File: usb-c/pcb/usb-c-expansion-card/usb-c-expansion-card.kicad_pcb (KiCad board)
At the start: 2 copper layers, 26 x 30 mm, 11 parts, among them P1 USB_C_Plug_USB2.0, U1 AP2112K-3.3

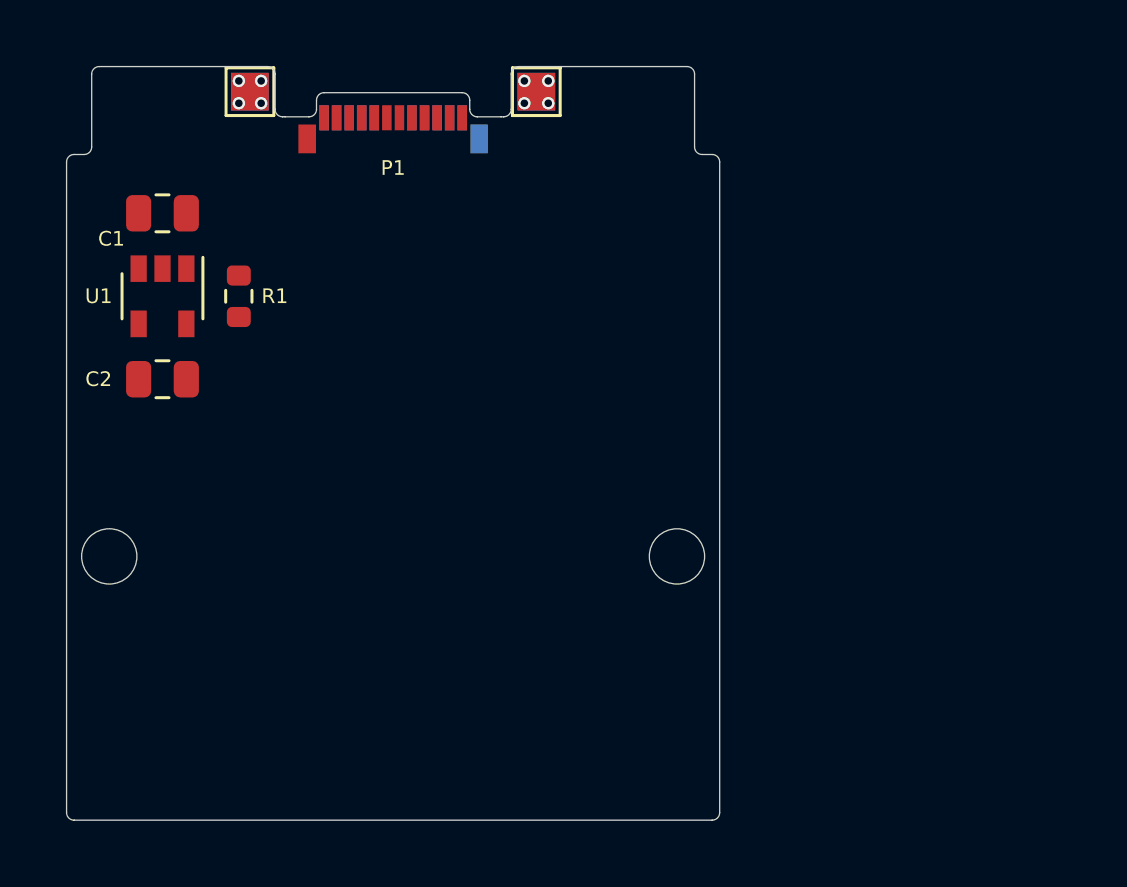
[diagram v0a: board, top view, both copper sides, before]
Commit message: Begin routing PCB
Signed-off-by: Lucy <user@domain.tld>
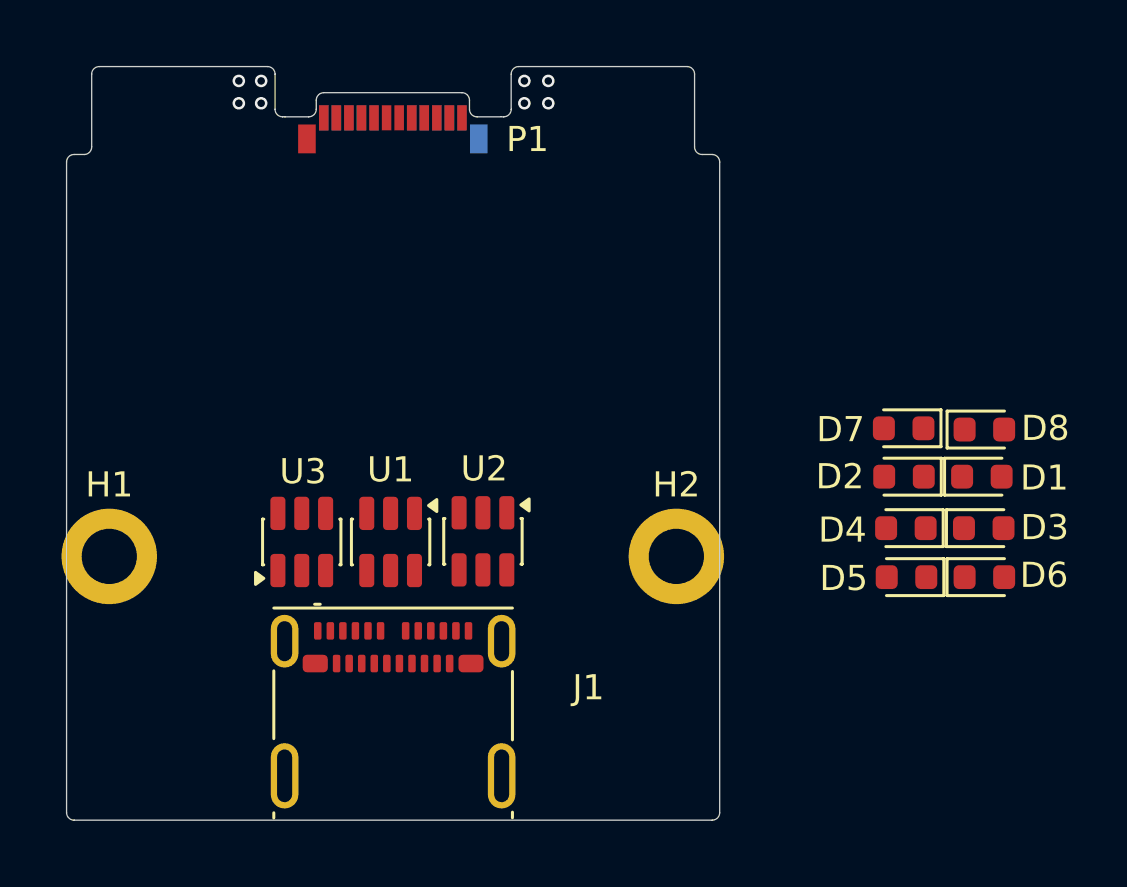
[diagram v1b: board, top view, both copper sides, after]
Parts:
- removed C1, C2: 10uF, Capacitor_SMD:C_0805_2012Metric
- removed R1: 5.1k, Resistor_SMD:R_0603_1608Metric
- removed TP1, TP2, TP3, TP4: TestPoint, TestPoint:TestPoint_Pad_1.5x1.5mm
- added D1: AZ5B0S-01F, Diode_SMD:D_0603_1608Metric, F.Cu at (163.4, 143.3)
- added D2: AZ5B0S-01F, Diode_SMD:D_0603_1608Metric, F.Cu at (160.3, 143.3)
- added D3: AZ5B0S-01F, Diode_SMD:D_0603_1608Metric, F.Cu at (163.5, 145.4)
- added D4: AZ5B0S-01F, Diode_SMD:D_0603_1608Metric, F.Cu at (160.4, 145.4)
- added D5: AZ5B0S-01F, Diode_SMD:D_0603_1608Metric, F.Cu at (160.4, 147.3)
- added D6: AZ5B0S-01F, Diode_SMD:D_0603_1608Metric, F.Cu at (163.5, 147.3)
- added D7: AZ5B0S-01F, Diode_SMD:D_0603_1608Metric, F.Cu at (160.3, 141.4)
- added D8: AZ5B0S-01F, Diode_SMD:D_0603_1608Metric, F.Cu at (163.5, 141.4)
- added J1: USB_C_Receptacle, Connector_USB:USB_C_Receptacle_Molex_105450-0101, F.Cu at (140.0, 152.7)
- added U2: USBLC6-2SC6, Package_TO_SOT_SMD:SOT-23-6, F.Cu at (143.6, 145.9)
- added U3: USBLC6-2SC6, Package_TO_SOT_SMD:SOT-23-6, F.Cu at (136.4, 145.9)
- H1, H2: footprint MountingHole:MountingHole_2.2mm_M2 -> MountingHole:MountingHole_2.2mm_M2_DIN965_Pad
- P1: value USB_C_Plug_USB2.0 -> USB_C_Plug
- U1: value AP2112K-3.3 -> USBLC6-2SC6; footprint Package_TO_SOT_SMD:SOT-23-5 -> Package_TO_SOT_SMD:SOT-23-6
- moved U1 13.3 mm to (139.9, 145.9)
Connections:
- P1 pad A10: (no net) -> /RX2N_ESD
- P1 pad A11: (no net) -> /RX2P_ESD
- P1 pad A2: (no net) -> /TX1P_ESD
- P1 pad A3: (no net) -> /TX1N_ESD
- P1 pad A4: VBUS -> /VBUS
- P1 pad A6: (no net) -> Net-(P1-D+)
- P1 pad A7: (no net) -> Net-(P1-D-)
- P1 pad A8: (no net) -> Net-(P1-SBU1)
- P1 pad A9: VBUS -> /VBUS
- P1 pad B10: (no net) -> /RX1N_ESD
- P1 pad B11: (no net) -> /RX1P_ESD
- P1 pad B2: (no net) -> /TX2P_ESD
- P1 pad B3: (no net) -> /TX2N_ESD
- P1 pad B4: VBUS -> /VBUS
- P1 pad B5: (no net) -> Net-(P1-VCONN)
- P1 pad B8: (no net) -> Net-(P1-SBU2)
- P1 pad B9: VBUS -> /VBUS
- P1 pad S1: GND -> (no net)
- U1 pad 1: VBUS -> Net-(P1-D-)
- U1 pad 3: VBUS -> Net-(P1-D+)
- U1 pad 4: (no net) -> Net-(J1-D+-PadA6)
- U1 pad 5: +3V3 -> unconnected-(U1-VBUS-Pad5)
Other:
- copper layers 2 -> 4
- net class Default removed

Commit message: Update net labels for differential pair routing
Signed-off-by: Lucy <user@domain.tld>
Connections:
- net /RX1N_ESD renamed /ESD_RX1_N
- net /RX1P_ESD renamed /ESD_RX1_P
- net /RX2N_ESD renamed /ESD_RX2_N
- net /RX2P_ESD renamed /ESD_RX2_P
- net /TX1N_ESD renamed /ESD_TX1_N
- net /TX1P_ESD renamed /ESD_TX1_P
- net /TX2N_ESD renamed /ESD_TX2_N
- net /TX2P_ESD renamed /ESD_TX2_P
- net Net-(J1-CC1) renamed /CC1
- net Net-(J1-CC2) renamed /CC2
- net Net-(J1-D+-PadA6) renamed /IN_D_P
- net Net-(J1-D--PadA7) renamed /IN_D_N
- net Net-(J1-SBU1) renamed /IN_SBU1
- net Net-(J1-SBU2) renamed /IN_SBU2
- net Net-(P1-CC) renamed /CC
- net Net-(P1-D+) renamed /OUT_D_P
- net Net-(P1-D-) renamed /OUT_D_N
- net Net-(P1-SBU1) renamed /OUT_SBU1
- net Net-(P1-SBU2) renamed /OUT_SBU2
- net Net-(P1-VCONN) renamed /VCONN
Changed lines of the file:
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@@
 		(13 "F.Paste" user)
 		(15 "B.Paste" user)
-		(5 "F.SilkS" user)
-		(7 "B.SilkS" user)
+		(5 "F.SilkS" user "F.Silkscreen")
+		(7 "B.SilkS" user "B.Silkscreen")
 		(1 "F.Mask" user)
 		(3 "B.Mask" user)
 		(25 "Edge.Cuts" user)
 		(27 "Margin" user)
-		(31 "F.CrtYd" user)
-		(29 "B.CrtYd" user)
+		(31 "F.CrtYd" user "F.Courtyard")
+		(29 "B.CrtYd" user "B.Courtyard")
 		(35 "F.Fab" user)
 	)
@@
 		(capping no)
 		(filling no)
-		(zone_defaults)
 		(pcbplotparams
 			(layerselection 0x00000000_00000000_55555555_57555550)
@@
 			(layers "F.Cu" "F.Mask" "F.Paste")
 			(roundrect_rratio 0.25)
-			(net "/TX1P_ESD")
+			(net "/ESD_TX1_P")
 			(pinfunction "A1_1")
 			(pintype "passive")
@@
 			(layers "F.Cu" "F.Mask" "F.Paste")
 			(roundrect_rratio 0.25)
-			(net "/RX1N_ESD")
+			(net "/ESD_RX1_N")
 			(pinfunction "A1_1")
 			(pintype "passive")
@@
 			(layers "F.Cu" "F.Mask" "F.Paste")
 			(roundrect_rratio 0.25)
-			(net "/TX2N_ESD")
+			(net "/ESD_TX2_N")
 			(pinfunction "A1_1")
 			(pintype "passive")
@@
 			(layers "F.Cu" "F.Mask" "F.Paste")
 			(roundrect_rratio 0.25)
-			(net "/TX1P_ESD")
+			(net "/ESD_TX1_P")
 			(pinfunction "TX1+_A2")
 			(pintype "bidirectional")
@@
 			(layers "F.Cu" "F.Mask" "F.Paste")
 			(roundrect_rratio 0.25)
-			(net "/TX1N_ESD")
+			(net "/ESD_TX1_N")
 			(pinfunction "TX1-_A3")
 			(pintype "bidirectional")
@@
 			(layers "F.Cu" "F.Mask" "F.Paste")
 			(roundrect_rratio 0.25)
-			(net "Net-(J1-CC1)")
+			(net "/CC1")
 			(pinfunction "CC1_A5")
 			(pintype "bidirectional")
@@
 			(layers "F.Cu" "F.Mask" "F.Paste")
 			(roundrect_rratio 0.25)
-			(net "Net-(J1-D+-PadA6)")
+			(net "/IN_D_P")
 			(pinfunction "D+_A6")
 			(pintype "bidirectional")
@@
 			(layers "F.Cu" "F.Mask" "F.Paste")
 			(roundrect_rratio 0.25)
-			(net "Net-(J1-D--PadA7)")
+			(net "/IN_D_N")
 			(pinfunction "D-_A7")
 			(pintype "bidirectional")
@@
 			(layers "F.Cu" "F.Mask" "F.Paste")
 			(roundrect_rratio 0.25)
-			(net "Net-(J1-SBU1)")
+			(net "/IN_SBU1")
 			(pinfunction "SBU1_A8")
 			(pintype "bidirectional")
@@
 			(layers "F.Cu" "F.Mask" "F.Paste")
 			(roundrect_rratio 0.25)
-			(net "/RX2N_ESD")
+			(net "/ESD_RX2_N")
 			(pinfunction "RX2-_A10")
 			(pintype "bidirectional")
@@
 			(layers "F.Cu" "F.Mask" "F.Paste")
 			(roundrect_rratio 0.25)
-			(net "/RX2P_ESD")
+			(net "/ESD_RX2_P")
 			(pinfunction "RX2+_A11")
 			(pintype "bidirectional")
@@
 			(layers "F.Cu" "F.Mask" "F.Paste")
 			(roundrect_rratio 0.25)
-			(net "/TX2P_ESD")
+			(net "/ESD_TX2_P")
 			(pinfunction "TX2+_B2")
 			(pintype "bidirectional")
@@
 			(layers "F.Cu" "F.Mask" "F.Paste")
 			(roundrect_rratio 0.25)
-			(net "/TX2N_ESD")
+			(net "/ESD_TX2_N")
 			(pinfunction "TX2-_B3")
 			(pintype "bidirectional")
@@
 			(layers "F.Cu" "F.Mask" "F.Paste")
 			(roundrect_rratio 0.25)
-			(net "Net-(J1-CC2)")
+			(net "/CC2")
 			(pinfunction "CC2_B5")
 			(pintype "bidirectional")
@@
 			(layers "F.Cu" "F.Mask" "F.Paste")
 			(roundrect_rratio 0.25)
-			(net "Net-(J1-D+-PadA6)")
+			(net "/IN_D_P")
 			(pinfunction "D+_B6")
 			(pintype "bidirectional")
@@
 			(layers "F.Cu" "F.Mask" "F.Paste")
 			(roundrect_rratio 0.25)
-			(net "Net-(J1-D--PadA7)")
+			(net "/IN_D_N")
 			(pinfunction "D-_B7")
 			(pintype "bidirectional")
@@
 			(layers "F.Cu" "F.Mask" "F.Paste")
 			(roundrect_rratio 0.25)
-			(net "Net-(J1-SBU2)")
+			(net "/IN_SBU2")
 			(pinfunction "SBU2_B8")
 			(pintype "bidirectional")
@@
 			(layers "F.Cu" "F.Mask" "F.Paste")
 			(roundrect_rratio 0.25)
-			(net "/RX1N_ESD")
+			(net "/ESD_RX1_N")
 			(pinfunction "RX1-_B10")
 			(pintype "bidirectional")
@@
 			(layers "F.Cu" "F.Mask" "F.Paste")
 			(roundrect_rratio 0.25)
-			(net "/RX1P_ESD")
+			(net "/ESD_RX1_P")
 			(pinfunction "RX1+_B11")
 			(pintype "bidirectional")
@@
 			(size 0.38 1)
 			(layers "F.Cu" "F.Mask" "F.Paste")
-			(net "/TX1P_ESD")
+			(net "/ESD_TX1_P")
 			(pinfunction "TX1+_A2")
 			(pintype "bidirectional")
@@
 			(size 0.38 1)
 			(layers "F.Cu" "F.Mask" "F.Paste")
-			(net "/TX1N_ESD")
+			(net "/ESD_TX1_N")
 			(pinfunction "TX1-_A3")
 			(pintype "bidirectional")
@@
 			(size 0.38 1)
 			(layers "F.Cu" "F.Mask" "F.Paste")
-			(net "Net-(P1-CC)")
+			(net "/CC")
 			(pinfunction "CC_A5")
 			(pintype "bidirectional")
@@
 			(size 0.38 1)
 			(layers "F.Cu" "F.Mask" "F.Paste")
-			(net "Net-(P1-D+)")
+			(net "/OUT_D_P")
 			(pinfunction "D+_A6")
 			(pintype "bidirectional")
@@
 			(size 0.38 1)
 			(layers "F.Cu" "F.Mask" "F.Paste")
-			(net "Net-(P1-D-)")
+			(net "/OUT_D_N")
 			(pinfunction "D-_A7")
 			(pintype "bidirectional")
@@
 			(size 0.38 1)
 			(layers "F.Cu" "F.Mask" "F.Paste")
-			(net "Net-(P1-SBU1)")
+			(net "/OUT_SBU1")
 			(pinfunction "SBU1_A8")
 			(pintype "bidirectional")
@@
 			(size 0.38 1)
 			(layers "F.Cu" "F.Mask" "F.Paste")
-			(net "/RX2N_ESD")
+			(net "/ESD_RX2_N")
 			(pinfunction "RX2-_A10")
 			(pintype "bidirectional")
@@
 			(size 0.38 1)
 			(layers "F.Cu" "F.Mask" "F.Paste")
-			(net "/RX2P_ESD")
+			(net "/ESD_RX2_P")
 			(pinfunction "RX2+_A11")
 			(pintype "bidirectional")
@@
 			(size 0.38 1)
 			(layers "B.Cu" "B.Mask" "B.Paste")
-			(net "/TX2P_ESD")
+			(net "/ESD_TX2_P")
 			(pinfunction "TX2+_B2")
 			(pintype "bidirectional")
@@
 			(size 0.38 1)
 			(layers "B.Cu" "B.Mask" "B.Paste")
-			(net "/TX2N_ESD")
+			(net "/ESD_TX2_N")
 			(pinfunction "TX2-_B3")
 			(pintype "bidirectional")
@@
 			(size 0.38 1)
 			(layers "B.Cu" "B.Mask" "B.Paste")
-			(net "Net-(P1-VCONN)")
+			(net "/VCONN")
 			(pinfunction "VCONN_B5")
 			(pintype "bidirectional")
@@
 			(size 0.38 1)
 			(layers "B.Cu" "B.Mask" "B.Paste")
-			(net "Net-(P1-SBU2)")
+			(net "/OUT_SBU2")
 			(pinfunction "SBU2_B8")
 			(pintype "bidirectional")
@@
 			(size 0.38 1)
 			(layers "B.Cu" "B.Mask" "B.Paste")
-			(net "/RX1N_ESD")
+			(net "/ESD_RX1_N")
 			(pinfunction "RX1-_B10")
 			(pintype "bidirectional")
@@
 			(size 0.38 1)
 			(layers "B.Cu" "B.Mask" "B.Paste")
-			(net "/RX1P_ESD")
+			(net "/ESD_RX1_P")
 			(pinfunction "RX1+_B11")
 			(pintype "bidirectional")
@@
 			(layers "F.Cu" "F.Mask" "F.Paste")
 			(roundrect_rratio 0.25)
-			(net "Net-(P1-CC)")
+			(net "/CC")
 			(pinfunction "I/O1_1")
 			(pintype "passive")
@@
 			(layers "F.Cu" "F.Mask" "F.Paste")
 			(roundrect_rratio 0.25)
-			(net "Net-(P1-VCONN)")
+			(net "/VCONN")
 			(pinfunction "I/O2_3")
 			(pintype "passive")
@@
 			(layers "F.Cu" "F.Mask" "F.Paste")
 			(roundrect_rratio 0.25)
-			(net "Net-(J1-CC2)")
+			(net "/CC2")
 			(pinfunction "I/O2_4")
 			(pintype "passive")
@@
 			(layers "F.Cu" "F.Mask" "F.Paste")
 			(roundrect_rratio 0.25)
-			(net "Net-(J1-CC1)")
+			(net "/CC1")
 			(pinfunction "I/O1_6")
 			(pintype "passive")
@@
 			(layers "F.Cu" "F.Mask" "F.Paste")
 			(roundrect_rratio 0.25)
-			(net "Net-(P1-SBU1)")
+			(net "/OUT_SBU1")
 			(pinfunction "I/O1_1")
 			(pintype "passive")
@@
 			(layers "F.Cu" "F.Mask" "F.Paste")
 			(roundrect_rratio 0.25)
-			(net "Net-(P1-SBU2)")
+			(net "/OUT_SBU2")
 			(pinfunction "I/O2_3")
 			(pintype "passive")
@@
 			(layers "F.Cu" "F.Mask" "F.Paste")
 			(roundrect_rratio 0.25)
-			(net "Net-(J1-SBU2)")
+			(net "/IN_SBU2")
 			(pinfunction "I/O2_4")
 			(pintype "passive")
@@
 			(layers "F.Cu" "F.Mask" "F.Paste")
 			(roundrect_rratio 0.25)
-			(net "Net-(J1-SBU1)")
+			(net "/IN_SBU1")
 			(pinfunction "I/O1_6")
 			(pintype "passive")
@@
 			(layers "F.Cu" "F.Mask" "F.Paste")
 			(roundrect_rratio 0.25)
-			(net "/RX2N_ESD")
+			(net "/ESD_RX2_N")
 			(pinfunction "A1_1")
 			(pintype "passive")
@@
 			(layers "F.Cu" "F.Mask" "F.Paste")
 			(roundrect_rratio 0.25)
-			(net "/TX2P_ESD")
+			(net "/ESD_TX2_P")
 			(pinfunction "A1_1")
 			(pintype "passive")
@@
 			(layers "F.Cu" "F.Mask" "F.Paste")
 			(roundrect_rratio 0.25)
-			(net "Net-(P1-D-)")
+			(net "/OUT_D_N")
 			(pinfunction "I/O1_1")
 			(pintype "passive")
@@
 			(layers "F.Cu" "F.Mask" "F.Paste")
 			(roundrect_rratio 0.25)
-			(net "Net-(P1-D+)")
+			(net "/OUT_D_P")
 			(pinfunction "I/O2_3")
 			(pintype "passive")
@@
 			(layers "F.Cu" "F.Mask" "F.Paste")
 			(roundrect_rratio 0.25)
-			(net "Net-(J1-D+-PadA6)")
+			(net "/IN_D_P")
 			(pinfunction "I/O2_4")
 			(pintype "passive")
@@
 			(layers "F.Cu" "F.Mask" "F.Paste")
 			(roundrect_rratio 0.25)
-			(net "Net-(J1-D--PadA7)")
+			(net "/IN_D_N")
 			(pinfunction "I/O1_6")
 			(pintype "passive")
@@
 			(layers "F.Cu" "F.Mask" "F.Paste")
 			(roundrect_rratio 0.25)
-			(net "/TX1N_ESD")
+			(net "/ESD_TX1_N")
 			(pinfunction "A1_1")
 			(pintype "passive")
@@
 			(layers "F.Cu" "F.Mask" "F.Paste")
 			(roundrect_rratio 0.25)
-			(net "/RX2P_ESD")
+			(net "/ESD_RX2_P")
 			(pinfunction "A1_1")
 			(pintype "passive")
@@
 			(layers "F.Cu" "F.Mask" "F.Paste")
 			(roundrect_rratio 0.25)
-			(net "/RX1P_ESD")
+			(net "/ESD_RX1_P")
 			(pinfunction "A1_1")
 			(pintype "passive")

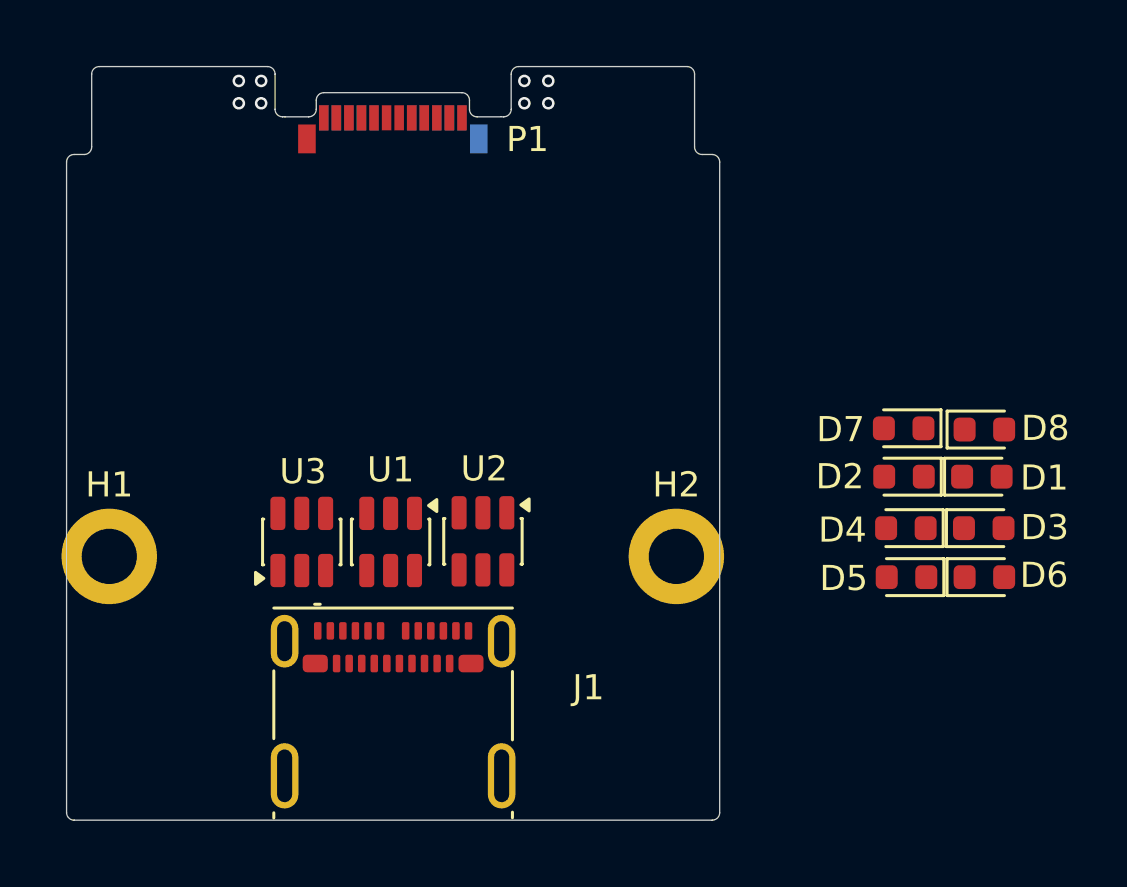
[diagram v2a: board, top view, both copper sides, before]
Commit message: first routing w/o ground planes finished
Signed-off-by: Lucy <user@domain.tld>
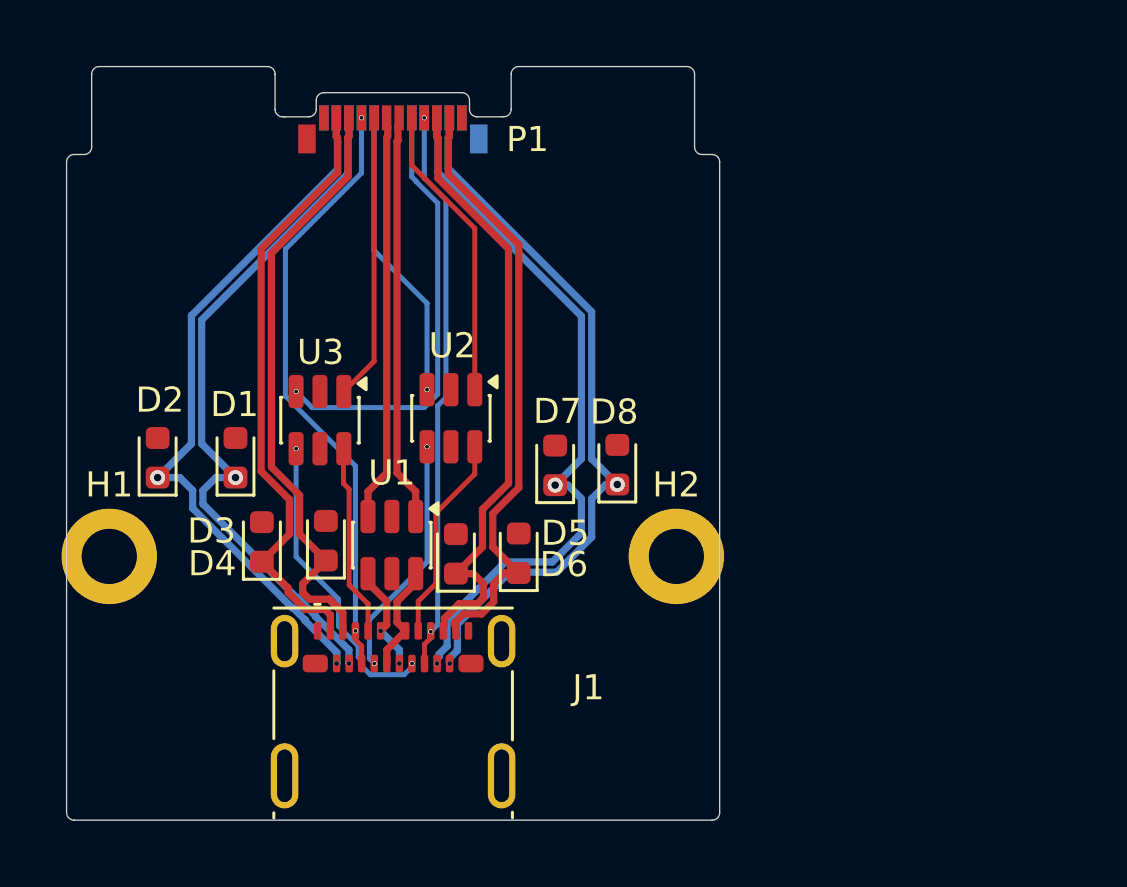
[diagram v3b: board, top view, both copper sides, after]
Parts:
- moved D1 29.7 mm to (133.7, 142.6), turned to 90 degrees
- moved D2 29.7 mm to (130.6, 142.6), turned to 90 degrees
- moved D3 26.2 mm to (137.3, 145.9), turned to 90 degrees
- moved D4 25.6 mm to (134.8, 145.9), turned to 90 degrees
- moved D6 18.6 mm to (145.0, 146.4), turned to 90 degrees
- moved D5 18.0 mm to (142.5, 146.4), turned to 90 degrees
- moved D8 14.7 mm to (148.9, 142.8), turned to 90 degrees
- moved D7 14.0 mm to (146.4, 142.9), turned to 90 degrees
- moved U2 5.06 mm to (142.3, 141.0)
- moved U3 4.90 mm to (137.1, 141.1), turned to -90 degrees
- moved U1 0.13 mm to (139.9, 146.1)
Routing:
- net /VBUS: track 0.00 -> 46.7 mm, vias 0 -> 4
- net /ESD_TX2_N: track 0.00 -> 28.8 mm, vias 0 -> 2
- net /ESD_TX2_P: track 0.00 -> 28.7 mm, vias 0 -> 2
- net /ESD_RX1_P: track 0.00 -> 28.2 mm, vias 0 -> 2
- net /ESD_RX1_N: track 0.00 -> 28.1 mm, vias 0 -> 2
- net /ESD_TX1_N: track 0.00 -> 24.6 mm
- net /ESD_RX2_N: track 0.00 -> 24.4 mm
- net /ESD_RX2_P: track 0.00 -> 24.3 mm
- net /ESD_TX1_P: track 0.00 -> 24.2 mm
- net /VCONN: track 0.00 -> 17.6 mm, vias 0 -> 1
- net /OUT_D_P: track 0.00 -> 16.2 mm
- net /OUT_D_N: track 0.00 -> 16.2 mm
- net /CC2: track 0.00 -> 12.1 mm, vias 0 -> 2
- net /OUT_SBU1: track 0.00 -> 11.9 mm
- net /OUT_SBU2: track 0.00 -> 11.7 mm, vias 0 -> 1
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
